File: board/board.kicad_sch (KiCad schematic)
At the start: 4 parts, among them J1 002_SPI, J2 012_CAN

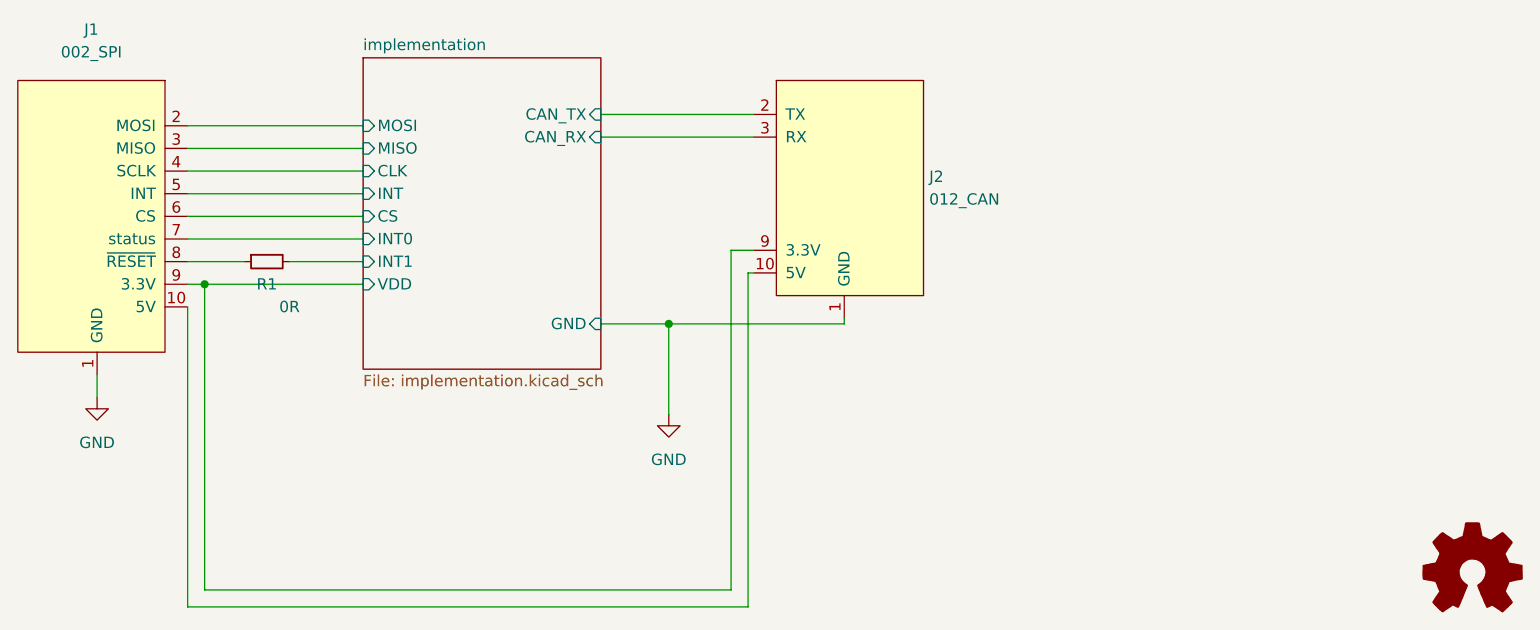
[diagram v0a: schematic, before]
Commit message: renamed subsheet to work better in compositions
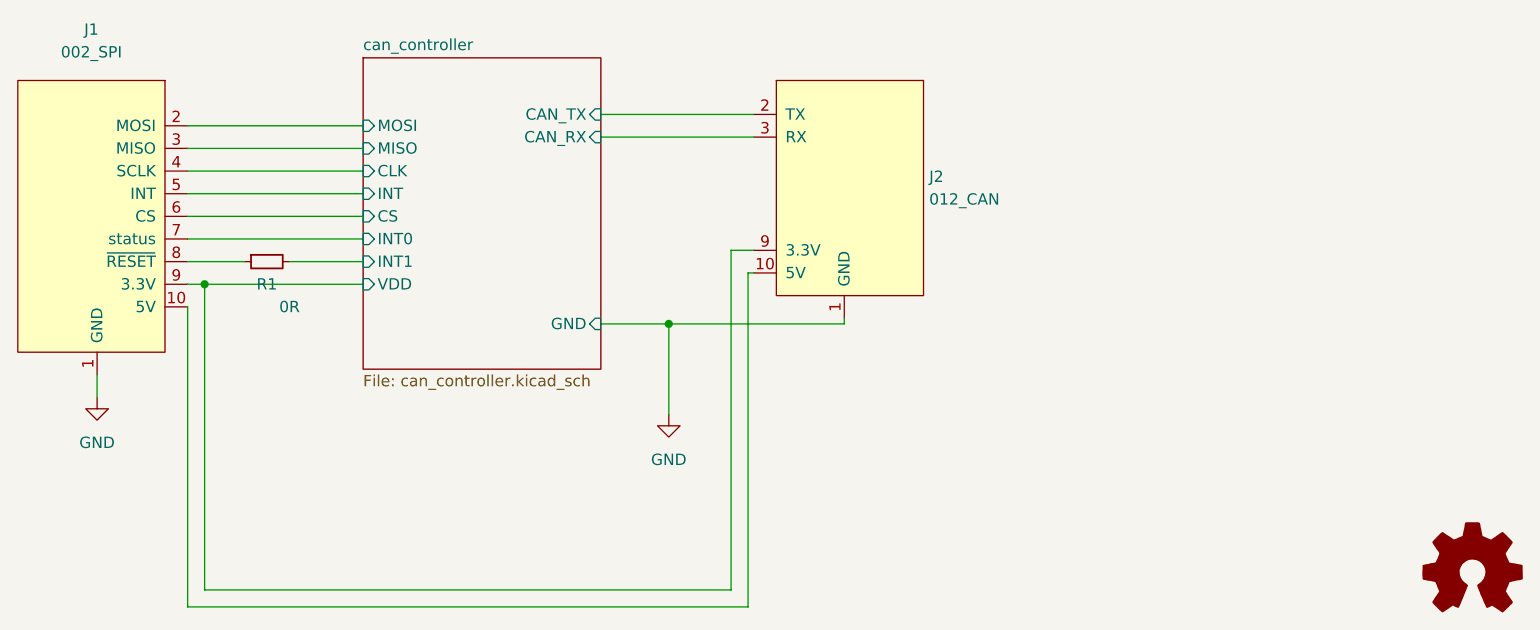
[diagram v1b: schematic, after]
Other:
- sheet implementation renamed can_controller
- sheet can_controller: file implementation.kicad_sch -> can_controller.kicad_sch
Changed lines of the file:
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@@
     (stroke (width 0.1524) (type solid) (color 0 0 0 0))
     (fill (color 0 0 0 0.0000))
-    (property "Sheet name" "implementation" (id 0) (at 148.59 98.9834 0)
+    (property "Sheet name" "can_controller" (id 0) (at 148.59 98.9834 0)
       (effects (font (size 1.27 1.27)) (justify left bottom))
     )
-    (property "Sheet file" "implementation.kicad_sch" (id 1) (at 148.59 135.2046 0)
+    (property "Sheet file" "can_controller.kicad_sch" (id 1) (at 148.59 135.2046 0)
       (effects (font (size 1.27 1.27)) (justify left top))
     )
